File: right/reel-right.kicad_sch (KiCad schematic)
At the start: 44 parts, among them J1 Conn_01x02, SW1 SW_Push, SW10 SW_Push, SW11 SW_Push, SW12 SW_Push, SW13 SW_Push, SW14 SW_Push, SW15 SW_Push, SW16 SW_Push, SW17 SW_Push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

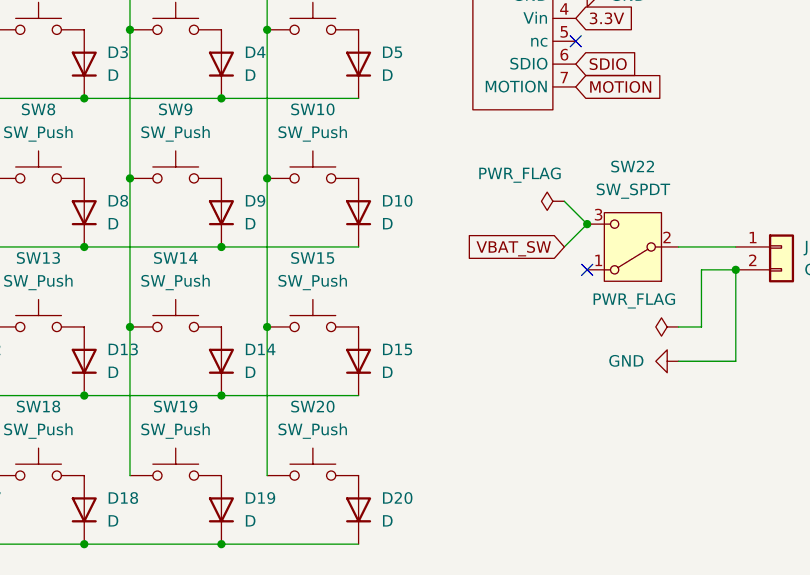
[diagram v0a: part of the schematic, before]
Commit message: Update left and right PCB layouts
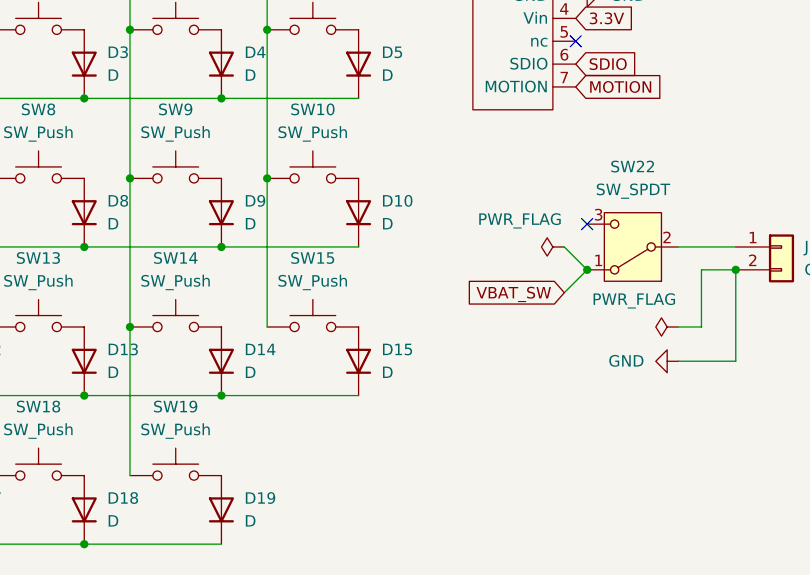
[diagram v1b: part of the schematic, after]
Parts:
- removed D20: D, Diode_SMD:D_SOD-123, symbol Device:D
- removed SW20: SW_Push, reel:SW_Hotswap_Kailh_Choc_V1_1.00u-NoClickHole, symbol Switch:SW_Push
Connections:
- net VBAT_SW: now also SW22.1 (A); no longer SW22.3 (C)
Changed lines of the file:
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@@
 	)
 	(junction
-		(at 87.63 162.56)
+		(at 128.27 132.08)
 		(diameter 0)
 		(color 0 0 0 0)
@@
 	)
 	(junction
-		(at 128.27 127)
-		(diameter 0)
-		(color 0 0 0 0)
-	)
-	(junction
 		(at 41.91 113.03)
 		(diameter 0)
@@
 	)
 	(junction
-		(at 92.71 138.43)
-		(diameter 0)
-		(color 0 0 0 0)
-	)
-	(junction
 		(at 72.39 146.05)
 		(diameter 0)
@@
 	)
 	(no_connect
+		(at 128.27 127)
+	)
+	(no_connect
 		(at 86.36 29.21)
 	)
@@
 	)
 	(no_connect
-		(at 128.27 132.08)
-	)
-	(no_connect
 		(at 39.37 33.02)
 	)
@@
 	(wire
 		(pts
-			(xy 125.73 124.46) (xy 128.27 127)
+			(xy 125.73 129.54) (xy 128.27 132.08)
 		)
 		(stroke
@@
 	(wire
 		(pts
-			(xy 87.63 162.56) (xy 102.87 162.56)
-		)
-		(stroke
-			(width 0)
-			(type default)
-		)
-	)
-	(wire
-		(pts
 			(xy 29.21 146.05) (xy 41.91 146.05)
 		)
@@
 	(wire
 		(pts
-			(xy 125.73 129.54) (xy 128.27 127)
+			(xy 125.73 134.62) (xy 128.27 132.08)
 		)
 		(stroke
@@
 	(wire
 		(pts
-			(xy 92.71 138.43) (xy 92.71 154.94)
-		)
-		(stroke
-			(width 0)
-			(type default)
-		)
-	)
-	(wire
-		(pts
 			(xy 29.21 162.56) (xy 41.91 162.56)
 		)
@@
 	(global_label "VBAT_SW"
 		(shape input)
-		(at 125.73 129.54 180)
+		(at 125.73 134.62 180)
 		(fields_autoplaced yes)
 		(effects
@@
 		)
 		(property "Intersheetrefs" "${INTERSHEET_REFS}"
-			(at 114.7015 129.54 0)
+			(at 114.7015 134.62 0)
 			(hide yes)
 			(show_name no)
@@
 	)
 	(symbol
-		(lib_id "Device:D")
-		(at 102.87 158.75 90)
-		(unit 1)
-		(body_style 1)
-		(exclude_from_sim no)
-		(in_bom yes)
-		(on_board yes)
-		(in_pos_files yes)
-		(dnp no)
-		(fields_autoplaced yes)
-		(property "Reference" "D20"
-			(at 105.41 157.4799 90)
-			(show_name no)
-			(do_not_autoplace no)
-			(effects
-				(font
-					(size 1.27 1.27)
-				)
-				(justify right)
-			)
-		)
-		(property "Value" "D"
-			(at 105.41 160.0199 90)
-			(show_name no)
-			(do_not_autoplace no)
-			(effects
-				(font
-					(size 1.27 1.27)
-				)
-				(justify right)
-			)
-		)
-		(property "Footprint" "Diode_SMD:D_SOD-123"
-			(at 102.87 158.75 0)
-			(hide yes)
-			(show_name no)
-			(do_not_autoplace no)
-			(effects
-				(font
-					(size 1.27 1.27)
-				)
-			)
-		)
-		(property "Datasheet" ""
-			(at 102.87 158.75 0)
-			(hide yes)
-			(show_name no)
-			(do_not_autoplace no)
-			(effects
-				(font
-					(size 1.27 1.27)
-				)
-			)
-		)
-		(property "Description" "Diode"
-			(at 102.87 158.75 0)
-			(hide yes)
-			(show_name no)
-			(do_not_autoplace no)
-			(effects
-				(font
-					(size 1.27 1.27)
-				)
-			)
-		)
-		(property "Sim.Device" "D"
-			(at 102.87 158.75 0)
-			(hide yes)
-			(show_name no)
-			(do_not_autoplace no)
-			(effects
-				(font
-					(size 1.27 1.27)
-				)
-			)
-		)
-		(property "Sim.Pins" "1=K 2=A"
-			(at 102.87 158.75 0)
-			(hide yes)
-			(show_name no)
-			(do_not_autoplace no)
-			(effects
-				(font
-					(size 1.27 1.27)
-				)
-			)
-		)
-		(pin "1"
-		)
-		(pin "2"
-		)
-		(instances
-			(project "reel-right"
-				(path "/d60071c6-f7f9-450c-8a0b-37b322aafb40"
-					(reference "D20")
-					(unit 1)
-				)
-			)
-		)
-	)
-	(symbol
 		(lib_id "smkbd_Library:XIAO-nRF52840_plus_maked_by_mki")
 		(at 29.21 21.59 0)
@@
 	)
 	(symbol
-		(lib_id "Switch:SW_Push")
-		(at 97.79 154.94 0)
-		(unit 1)
-		(body_style 1)
-		(exclude_from_sim no)
-		(in_bom yes)
-		(on_board yes)
-		(in_pos_files yes)
-		(dnp no)
-		(fields_autoplaced yes)
-		(property "Reference" "SW20"
-			(at 97.79 147.32 0)
-			(show_name no)
-			(do_not_autoplace no)
-			(effects
-				(font
-					(size 1.27 1.27)
-				)
-			)
-		)
-		(property "Value" "SW_Push"
-			(at 97.79 149.86 0)
-			(show_name no)
-			(do_not_autoplace no)
-			(effects
-				(font
-					(size 1.27 1.27)
-				)
-			)
-		)
-		(property "Footprint" "reel:SW_Hotswap_Kailh_Choc_V1_1.00u-NoClickHole"
-			(at 97.79 149.86 0)
-			(hide yes)
-			(show_name no)
-			(do_not_autoplace no)
-			(effects
-				(font
-					(size 1.27 1.27)
-				)
-			)
-		)
-		(property "Datasheet" ""
-			(at 97.79 149.86 0)
-			(hide yes)
-			(show_name no)
-			(do_not_autoplace no)
-			(effects
-				(font
-					(size 1.27 1.27)
-				)
-			)
-		)
-		(property "Description" "Push button switch, generic, two pins"
-			(at 97.79 154.94 0)
-			(hide yes)
-			(show_name no)
-			(do_not_autoplace no)
-			(effects
-				(font
-					(size 1.27 1.27)
-				)
-			)
-		)
-		(pin "2"
-		)
-		(pin "1"
-		)
-		(instances
-			(project "reel-right"
-				(path "/d60071c6-f7f9-450c-8a0b-37b322aafb40"
-					(reference "SW20")
-					(unit 1)
-				)
-			)
-		)
-	)
-	(symbol
 		(lib_id "power:GND")
 		(at 59.69 25.4 180)
@@
 	(symbol
 		(lib_id "power:PWR_FLAG")
-		(at 125.73 124.46 90)
+		(at 125.73 129.54 90)
 		(unit 1)
 		(body_style 1)
@@
 		(dnp no)
 		(property "Reference" "#FLG01"
-			(at 123.825 124.46 0)
+			(at 123.825 129.54 0)
 			(hide yes)
 			(show_name no)
@@
 		)
 		(property "Value" "PWR_FLAG"
-			(at 125.476 121.412 90)
+			(at 125.476 126.492 90)
 			(show_name no)
 			(do_not_autoplace no)
@@
 		)
 		(property "Footprint" ""
-			(at 125.73 124.46 0)
+			(at 125.73 129.54 0)
 			(hide yes)
 			(show_name no)
@@
 		)
 		(property "Datasheet" ""
-			(at 125.73 124.46 0)
+			(at 125.73 129.54 0)
 			(hide yes)
 			(show_name no)
@@
 		)
 		(property "Description" "Special symbol for telling ERC where power comes from"
-			(at 125.73 124.46 0)
+			(at 125.73 129.54 0)
 			(hide yes)
 			(show_name no)
